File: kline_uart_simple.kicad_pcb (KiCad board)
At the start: 4 copper layers, 9 parts, among them J1 USB2UART, J2 KLINE_CONN, Q1 BC547, Q2 BC547

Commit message: new output pdf
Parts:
- moved Q2 105.3 mm to (25.3, 19.8)
- moved R2 105.3 mm to (33.0, 23.4)
- moved R4 105.3 mm to (37.5, 26.3)
- moved R5 105.3 mm to (37.4, 32.8)
- moved J1 105.3 mm to (19.0, 32.5)
- moved J2 105.3 mm to (46.5, 20.9)
- moved Q1 105.3 mm to (31.4, 26.7)
- moved R1 105.3 mm to (24.8, 25.7)
- moved R3 105.3 mm to (37.5, 23.0)

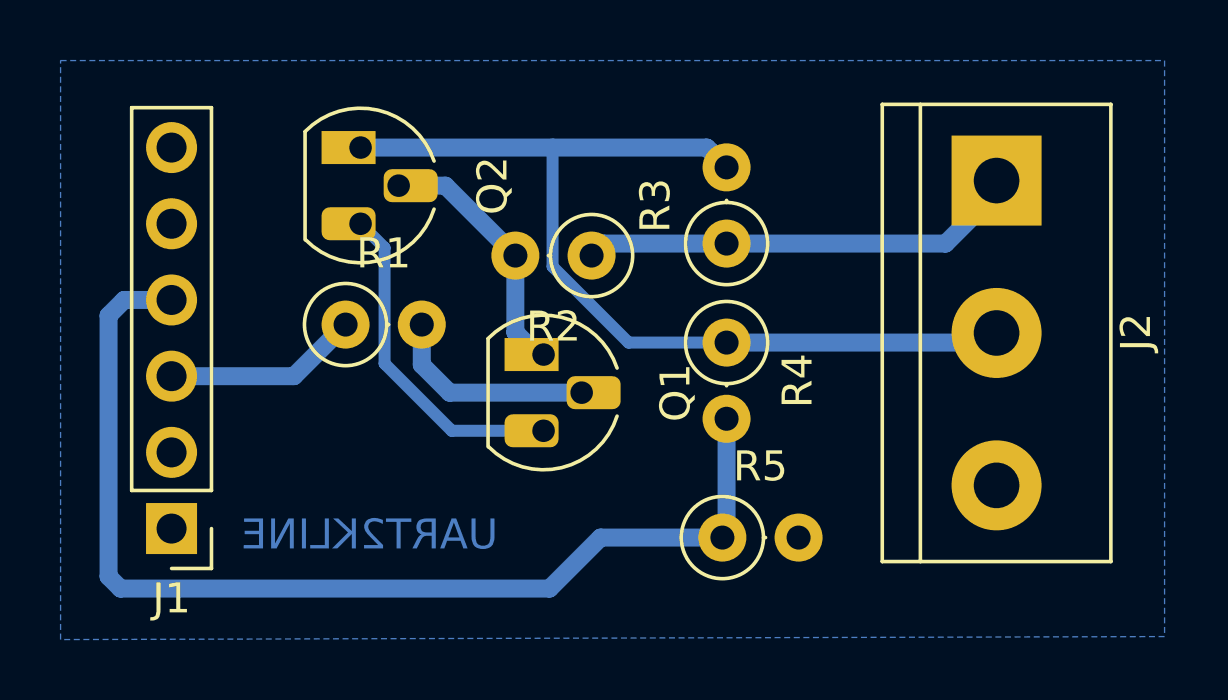
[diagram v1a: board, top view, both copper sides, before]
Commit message: Updated to kicad 6.0.2
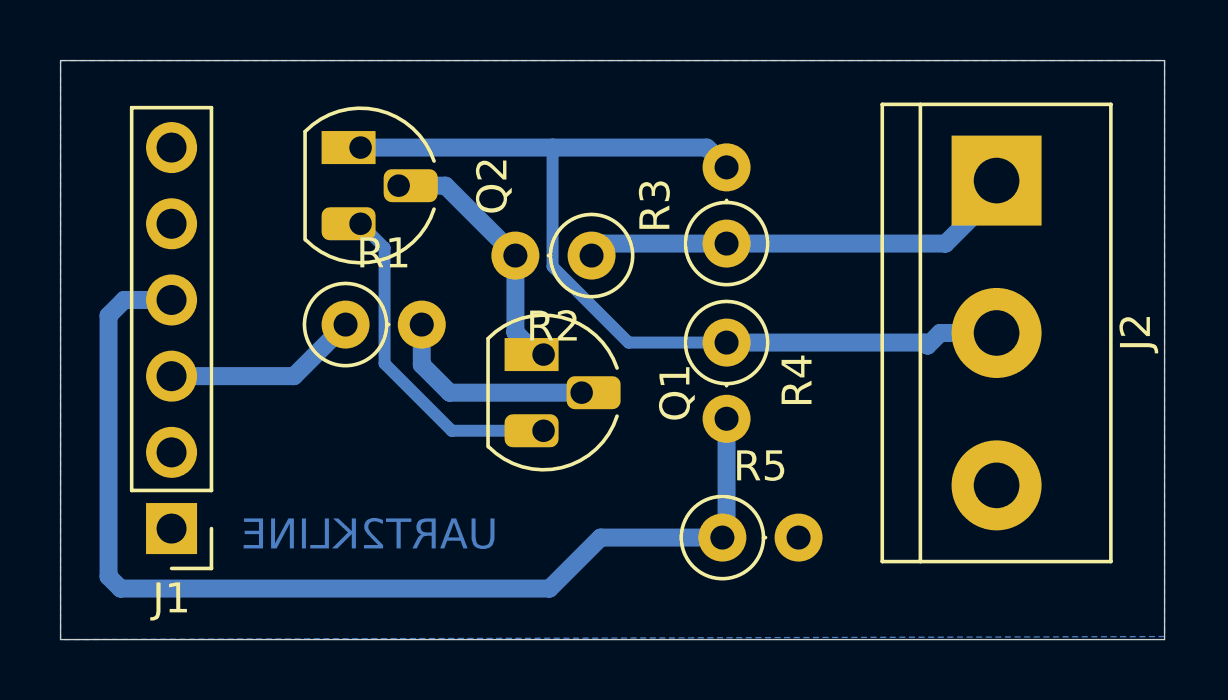
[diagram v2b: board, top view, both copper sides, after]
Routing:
- net KLINE: track 33.8 -> 34.3 mm
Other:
- board outline added: 36.8 x 19.3 mm
- net class Default removed

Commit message: New output files
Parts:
- moved R4 8.64 mm to (32.3, 19.4)
- moved J2 8.64 mm to (41.3, 14.0)
- moved R3 8.64 mm to (32.3, 16.1)
- moved R5 8.64 mm to (32.2, 25.9)
- moved Q2 8.64 mm to (20.1, 12.9)
- moved J1 8.64 mm to (13.8, 25.6)
- moved Q1 8.64 mm to (26.2, 19.8)
- moved R1 8.64 mm to (19.6, 18.8)
- moved R2 8.64 mm to (27.8, 16.5)
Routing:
- net KLINE: track 34.3 -> 33.8 mm
